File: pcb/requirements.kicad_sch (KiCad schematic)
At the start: 0 parts

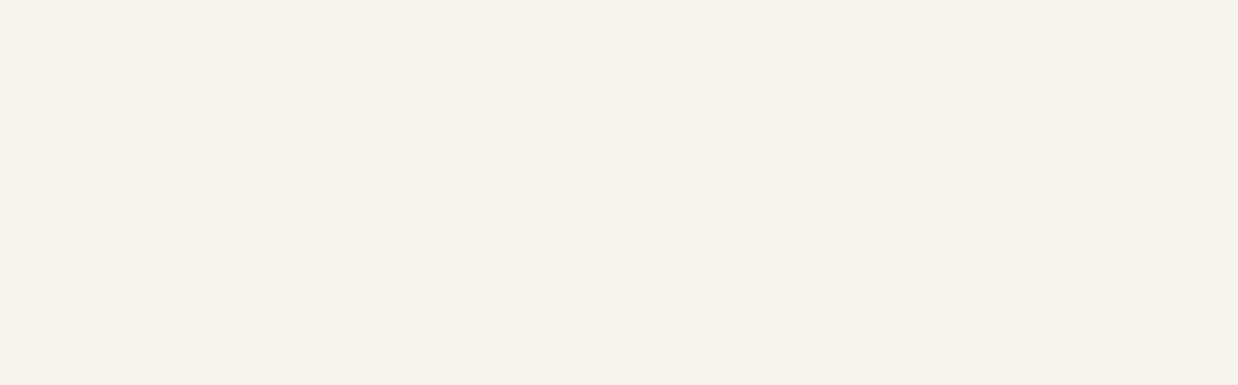
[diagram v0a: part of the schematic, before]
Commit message: Updated to latest libraries
Changed to all CRG footprints (mostly)
Moved somethings around
Added LED jumper
Updated symbols/logos
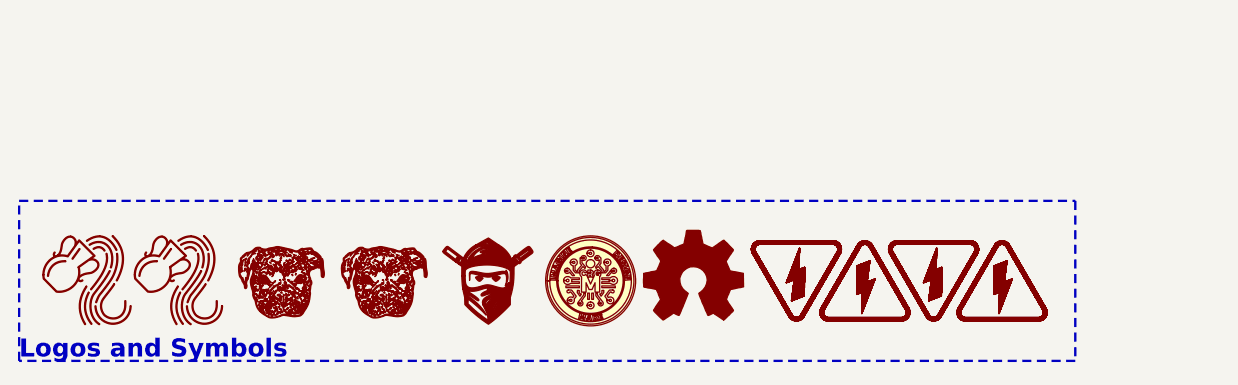
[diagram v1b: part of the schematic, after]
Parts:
- added LOGO1, LOGO3: ~, CRGM Logos:Aquarius Logo 8mm, symbol CRGM Logos:Aquarius Logo
- added LOGO2: ~, CRGM Logos:CRGM Logo 7mm, symbol CRGM Logos:CRGM Logo
- added LOGO4, LOGO6: ~, CRGM Logos:Roxy 8mm, symbol CRGM Logos:Roxy Logo
- added LOGO5: ~, Symbol:OSHW-Logo_5.7x6mm_SilkScreen, symbol Graphic:Logo_Open_Hardware_Small
- added LOGO7: ~, CRGM Logos:FNWW Face 8mm, symbol CRGM Logos:FNWW Face
- added S1, S2, S3, S4: ~, CRGM Symbols:HIGH-VOLTAGE-5MM, symbol CRGM Symbols:High Voltage
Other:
- note added: "Logos and Symbols"

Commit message: Updated for consistency
Updated footprints
Added ESD to power
Added second QWICC connector
Rerouted as required
Made mounting holes grounded
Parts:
- added H1, H2, H3, H4: MountingHole, CRGM Mechanical:MountingHole_3.2mm_M3_Pad_Via, symbol CRGM Mechanical:MountingHole_Pad
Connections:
- new net GND: H1.1, H2.1
- no-connect marks 0 -> 2
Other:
- note added: "Mechanical"

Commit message: Updated parts and models
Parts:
- LOGO3: footprint CRGM Logos:Aquarius Logo 8mm -> CRGM Logos:Aquarius Logo 5mm
- LOGO4: footprint CRGM Logos:Roxy 8mm -> CRGM Logos:Roxy 5mm
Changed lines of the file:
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@@
 		)
 	)
-	(text_box "PCB:\n4 Layers\nThickness: 1.6mm\nCopper: 1oz\nFinish: HASL\nSoldermask: Purple\nSilkscreen: White\nMin Trace: 6mil\nMin Spacing: 5mil\nMin Drill: 0.25mm\nMin Via: 0.3mm\nMin Via Annular Ring: 0.6mm\n\n"
+	(text_box "PCB:\n4 Layers\nThickness: 1.6mm\nCopper: 1oz (2oz maybe required)\nFinish: HASL\nSoldermask: Purple\nSilkscreen: White\nMin Trace: 6mil\nMin Spacing: 5mil\nMin Drill: 0.25mm\nMin Via: 0.3mm\nMin Via Annular Ring: 0.6mm\n\n"
 		(exclude_from_sim yes)
 		(at 106.68 92.71 0)
@@
 		)
 	)
-	(text_box "BASIC\n\n* ATTiny1616 Process\n* Adafruit Seesaw Protocol\n* One relay\n* Power In/Out Ports\n* Optional Pull Ups for I2C\n* I2C Address Selection (2-bits)\n* Flyback Diode for Relay"
+	(text_box "BASIC\n\n* ATTiny1616 Process\n* Adafruit Seesaw Protocol\n* One relay; optically isolated\n* Power In/Out Ports\n* Optional Pull Ups for I2C\n* I2C Address Selection (2-bits)\n* Flyback Diode for Relay"
 		(exclude_from_sim yes)
 		(at 19.05 31.75 0)
@@
 			)
 		)
-		(property "Footprint" "CRGM Logos:Aquarius Logo 8mm"
+		(property "Footprint" "CRGM Logos:Aquarius Logo 5mm"
 			(at 32.004 191.008 0)
 			(effects
@@
 			)
 		)
-		(property "Footprint" "CRGM Logos:Roxy 8mm"
+		(property "Footprint" "CRGM Logos:Roxy 5mm"
 			(at 41.91 196.088 0)
 			(effects

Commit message: Updated I2C pulls to open jumper
Fixed I2C to be open rather than bridged.
Changed opto-isolator to CRGM library.
Updated picture of bottom side to match new footprint
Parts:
- LOGO2: now left out of the parts list
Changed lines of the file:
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@@
+			)
+		)
+		(property "Sim.Enable" ""
+			(at 163.83 170.18 90)
+			(effects
+				(font
+					(size 1.27 1.27)
+				)
+				(hide yes)
 			)
 		)
@@
 			)
 		)
+		(property "Sim.Enable" ""
+			(at 99.06 187.96 0)
+			(effects
+				(font
+					(size 1.27 1.27)
+				)
+				(hide yes)
+			)
+		)
 		(instances
 			(project "relay-module"
@@
 			)
 		)
+		(property "Sim.Enable" ""
+			(at 20.32 187.96 0)
+			(effects
+				(font
+					(size 1.27 1.27)
+				)
+				(hide yes)
+			)
+		)
 		(instances
 			(project "relay-module"
@@
 			)
 		)
+		(property "Sim.Enable" ""
+			(at 114.3 187.96 0)
+			(effects
+				(font
+					(size 1.27 1.27)
+				)
+				(hide yes)
+			)
+		)
 		(instances
 			(project "relay-module"
@@
 		(property "MPN" ""
 			(at 163.83 180.34 0)
+			(effects
+				(font
+					(size 1.27 1.27)
+				)
+				(hide yes)
+			)
+		)
+		(property "Sim.Enable" ""
+			(at 163.83 180.34 90)
 			(effects
 				(font
@@
 			)
 		)
+		(property "Sim.Enable" ""
+			(at 87.63 187.96 0)
+			(effects
+				(font
+					(size 1.27 1.27)
+				)
+				(hide yes)
+			)
+		)
 		(instances
 			(project "relay-module"
@@
 			)
 		)
+		(property "Sim.Enable" ""
+			(at 64.77 187.96 0)
+			(effects
+				(font
+					(size 1.27 1.27)
+				)
+				(hide yes)
+			)
+		)
 		(instances
 			(project "relay-module"
@@
 		)
 		(property "Mouser" ""
+			(at 53.34 187.96 0)
+			(effects
+				(font
+					(size 1.27 1.27)
+				)
+				(hide yes)
+			)
+		)
+		(property "Sim.Enable" ""
 			(at 53.34 187.96 0)
 			(effects
@@
 			)
 		)
+		(property "Sim.Enable" ""
+			(at 30.48 187.96 0)
+			(effects
+				(font
+					(size 1.27 1.27)
+				)
+				(hide yes)
+			)
+		)
 		(instances
 			(project "relay-module"
@@
 		(unit 1)
 		(exclude_from_sim no)
-		(in_bom yes)
+		(in_bom no)
 		(on_board yes)
 		(dnp no)
@@
 		)
 		(property "Mouser" ""
+			(at 76.2 187.96 0)
+			(effects
+				(font
+					(size 1.27 1.27)
+				)
+				(hide yes)
+			)
+		)
+		(property "Sim.Enable" ""
 			(at 76.2 187.96 0)
 			(effects
@@
 			)
 		)
+		(property "Sim.Enable" ""
+			(at 106.68 187.96 0)
+			(effects
+				(font
+					(size 1.27 1.27)
+				)
+				(hide yes)
+			)
+		)
 		(instances
 			(project "relay-module"
@@
 		(property "Mouser" ""
 			(at 163.83 175.26 0)
+			(effects
+				(font
+					(size 1.27 1.27)
+				)
+				(hide yes)
+			)
+		)
+		(property "Sim.Enable" ""
+			(at 163.83 175.26 90)
 			(effects
 				(font
@@
 			)
 		)
+		(property "Sim.Enable" ""
+			(at 121.92 187.96 0)
+			(effects
+				(font
+					(size 1.27 1.27)
+				)
+				(hide yes)
+			)
+		)
 		(instances
 			(project "relay-module"
@@
 			)
 		)
+		(property "Sim.Enable" ""
+			(at 41.91 187.96 0)
+			(effects
+				(font
+					(size 1.27 1.27)
+				)
+				(hide yes)
+			)
+		)
 		(instances
 			(project "relay-module"
@@
 			(effects
 				(font
+					(size 1.27 1.27)
+				)
+				(hide yes)
+			)
+		)
+		(property "Sim.Enable" ""
+			(at 163.83 185.42 90)
+			(effects
+				(font
